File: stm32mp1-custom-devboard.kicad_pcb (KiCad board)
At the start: 4 copper layers, 120 x 72 mm, 124 parts, among them Con1 52746-0671, Con2 505110-2491, Con3 2041119-1, Con4 USB_C_Wurth_632723130112, Con5 USB_C_Wurth_632723130112, P1 Main Power Supply, Q1 BC847B, T2 WE-RJ45_74990101210, U1 TPS61169DCKR, U2 MCP1703T-3302E, U3 ST1S10PHR, U4 ST1S09IPUR, U5 STM32F103C(8-B)Tx, U6 MCP1700T-3302E_MB, U7 KSZ8041NL_RNL, X1 8.000MHZ, X2 ECS-2016MV-250-CN-TR

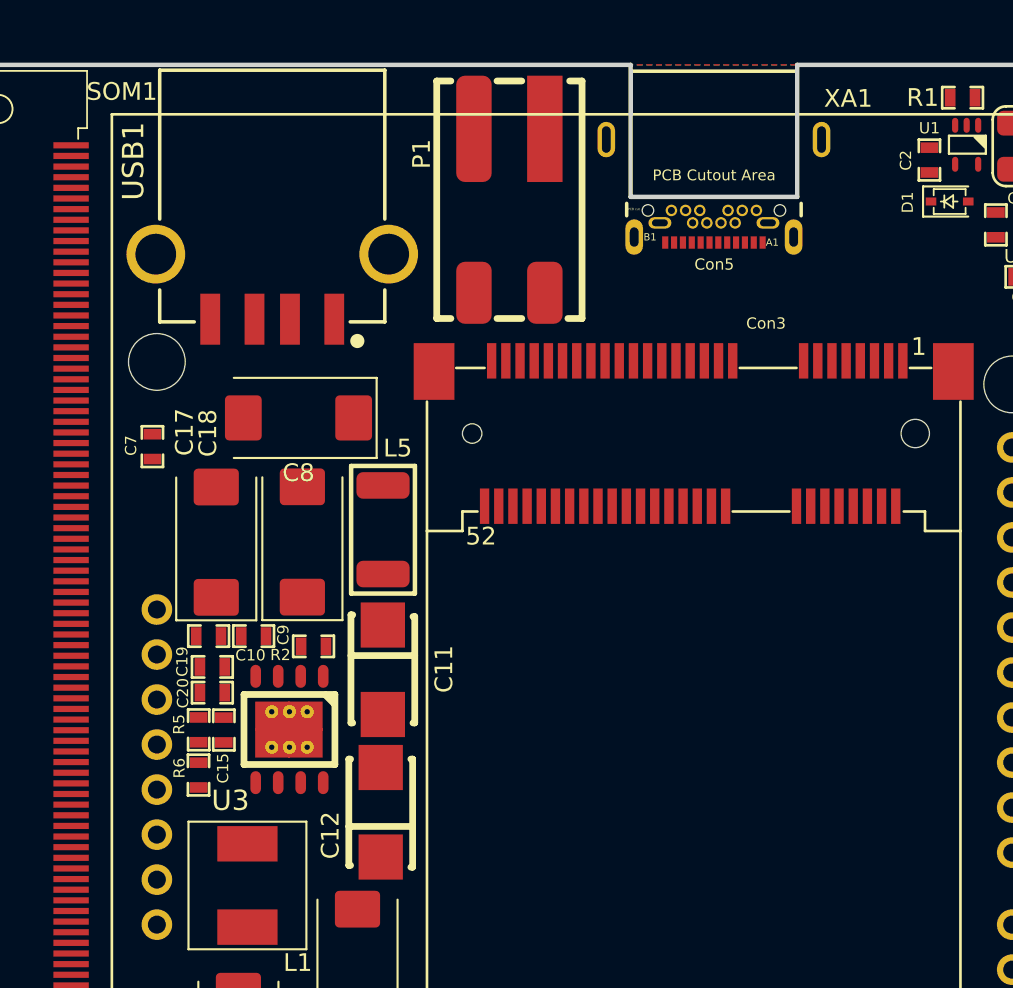
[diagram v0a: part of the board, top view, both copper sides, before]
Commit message: Updated schematic, added some components, figurated components on pcb
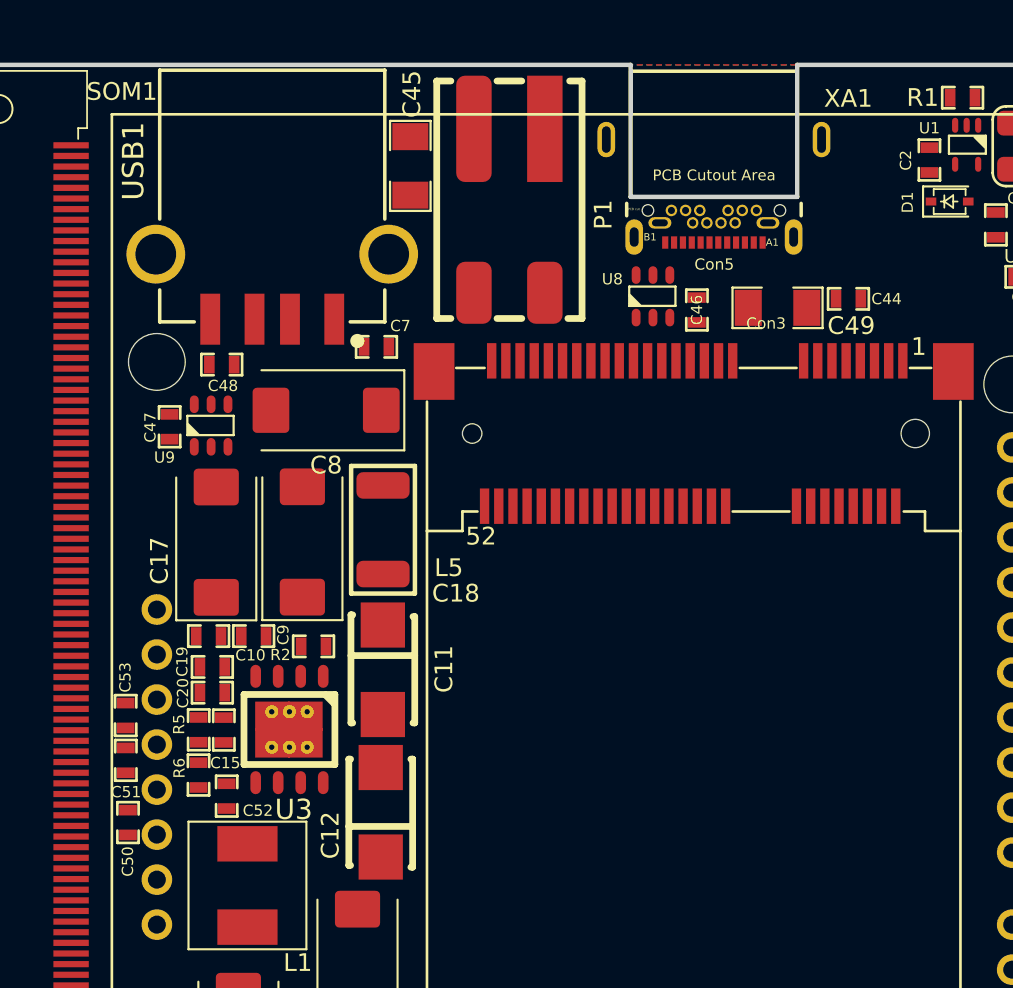
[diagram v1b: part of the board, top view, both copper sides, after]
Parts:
- added C44: 10uF, Capacitors_Smd_0603:10uF_10V_0603, F.Cu at (172.8, 79.6)
- added C45: 1nF/2kV, Capacitors_Smd_1206:1nF_2kV_1206, F.Cu at (148.0, 72.1)
- added C46: 100n, Capacitors_Smd_0603:100nF_0603, F.Cu at (164.2, 80.2)
- added C47: 10uF, Capacitors_Smd_0603:10uF_10V_0603, F.Cu at (134.5, 86.8)
- added C48: 100n, Capacitors_Smd_0603:100nF_0603, F.Cu at (137.4, 83.3)
- added C49: 1nF/2kV, Capacitors_Smd_1206:1nF_2kV_1206, F.Cu at (168.8, 80.1)
- added C50: 10uF, Capacitors_Smd_0603:10uF_10V_0603, F.Cu at (132.1, 109.2)
- added C51: 10uF, Capacitors_Smd_0603:10uF_10V_0603, F.Cu at (132.0, 105.7)
- added C52: 100n, Capacitors_Smd_0603:100nF_0603, F.Cu at (137.7, 107.7)
- added C53: 100n, Capacitors_Smd_0603:100nF_0603, F.Cu at (132.0, 103.1)
- added U8: USBLC6-2, ESD_Protectors:USBLC6-2_SOT23-6L, F.Cu at (161.7, 79.5)
- added U9: USBLC6-2, ESD_Protectors:USBLC6-2_SOT23-6L, F.Cu at (136.8, 86.8)
- moved C7 13.8 mm to (146.1, 82.3), turned to 180 degrees
- moved C8 1.62 mm to (143.3, 85.9)
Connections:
- net SHDN renamed Net-(C26-Pad2)
- C13 pad 1: /Power Supply Module/POWER_IN_7_TO_18V -> VPP
- C14 pad 1: /Power Supply Module/POWER_IN_7_TO_18V -> VPP
- C7 pad 1: /Power Supply Module/POWER_IN_7_TO_18V -> VPP
- C8 pad 1: /Power Supply Module/POWER_IN_7_TO_18V -> VPP
- Con5 pad A1: (no net) -> GND
- Con5 pad A12: (no net) -> GND
- Con5 pad A4: (no net) -> 5V
- Con5 pad A6: (no net) -> Net-(Con5-PadA6)
- Con5 pad A7: (no net) -> Net-(Con5-PadA7)
- Con5 pad A9: (no net) -> 5V
- Con5 pad B1: (no net) -> GND
- Con5 pad B12: (no net) -> GND
- Con5 pad B4: (no net) -> 5V
- Con5 pad B6: (no net) -> Net-(Con5-PadA6)
- Con5 pad B7: (no net) -> Net-(Con5-PadA7)
- Con5 pad B9: (no net) -> 5V
- Con5 pad S1: (no net) -> Net-(C49-Pad2)
- Con5 pad S2: (no net) -> Net-(C49-Pad2)
- Con5 pad S3: (no net) -> Net-(C49-Pad2)
- Con5 pad S4: (no net) -> Net-(C49-Pad2)
- L5 pad 1: /Power Supply Module/POWER_IN_7_TO_18V -> VPP
- P1 pad 2: /Power Supply Module/POWER_IN_7_TO_18V -> VPP
- U4 pad 4: /Power Supply Module/POWER_IN_7_TO_18V -> VPP
- U4 pad 5: /Power Supply Module/POWER_IN_7_TO_18V -> VPP
- U4 pad 6: /Power Supply Module/POWER_IN_7_TO_18V -> VPP
- USB1 pad 1: (no net) -> 5V
- USB1 pad 2: (no net) -> Net-(U9-Pad6)
- USB1 pad 3: (no net) -> Net-(U9-Pad4)
- USB1 pad 4: (no net) -> GND
- XA1 pad 3V3: (no net) -> 3V3
- XA1 pad 5V1: (no net) -> 5V
- XA1 pad 5V2: (no net) -> 5V
- XA1 pad GND1: (no net) -> GND
- XA1 pad GND2: (no net) -> GND
- XA1 pad GND3: (no net) -> GND
- XA1 pad GND4: (no net) -> GND
- XA1 pad VIN: (no net) -> VPP

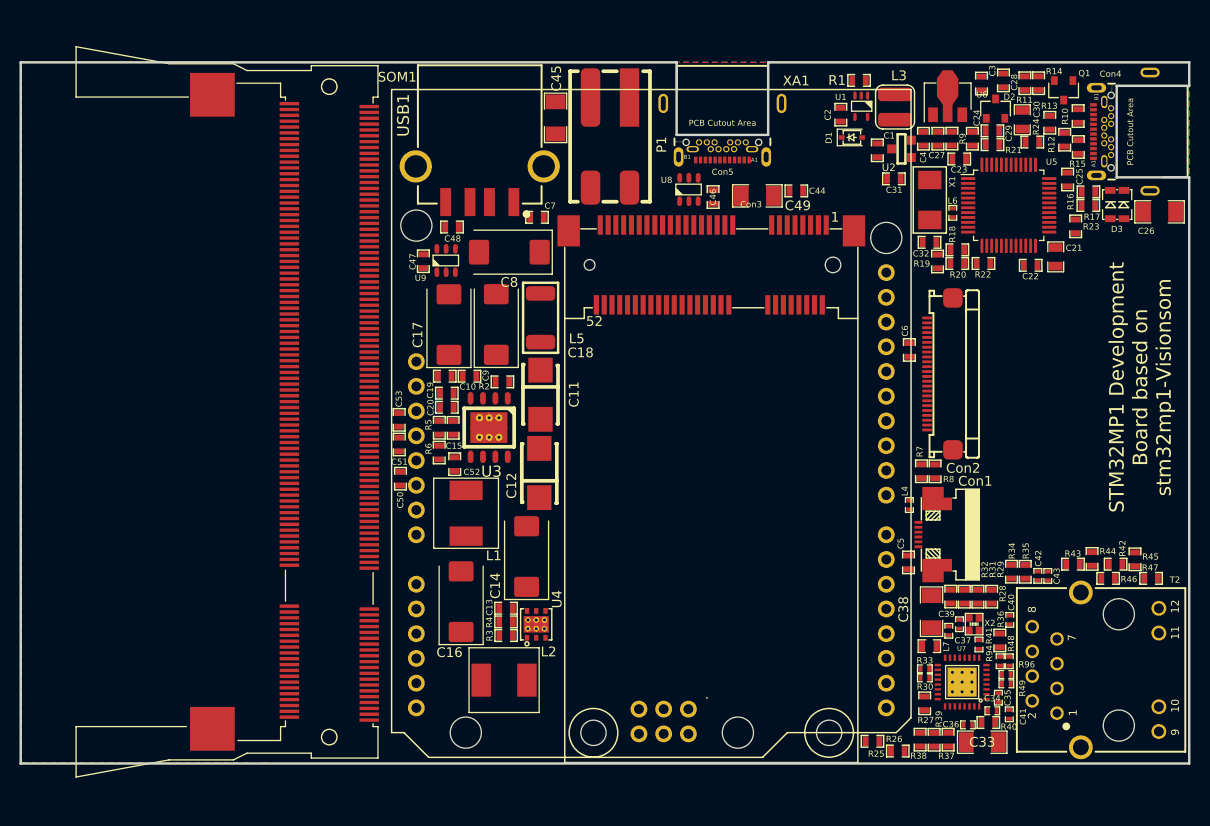
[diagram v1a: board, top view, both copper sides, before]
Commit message: Schematic work contiune, added pinout spreadsheet
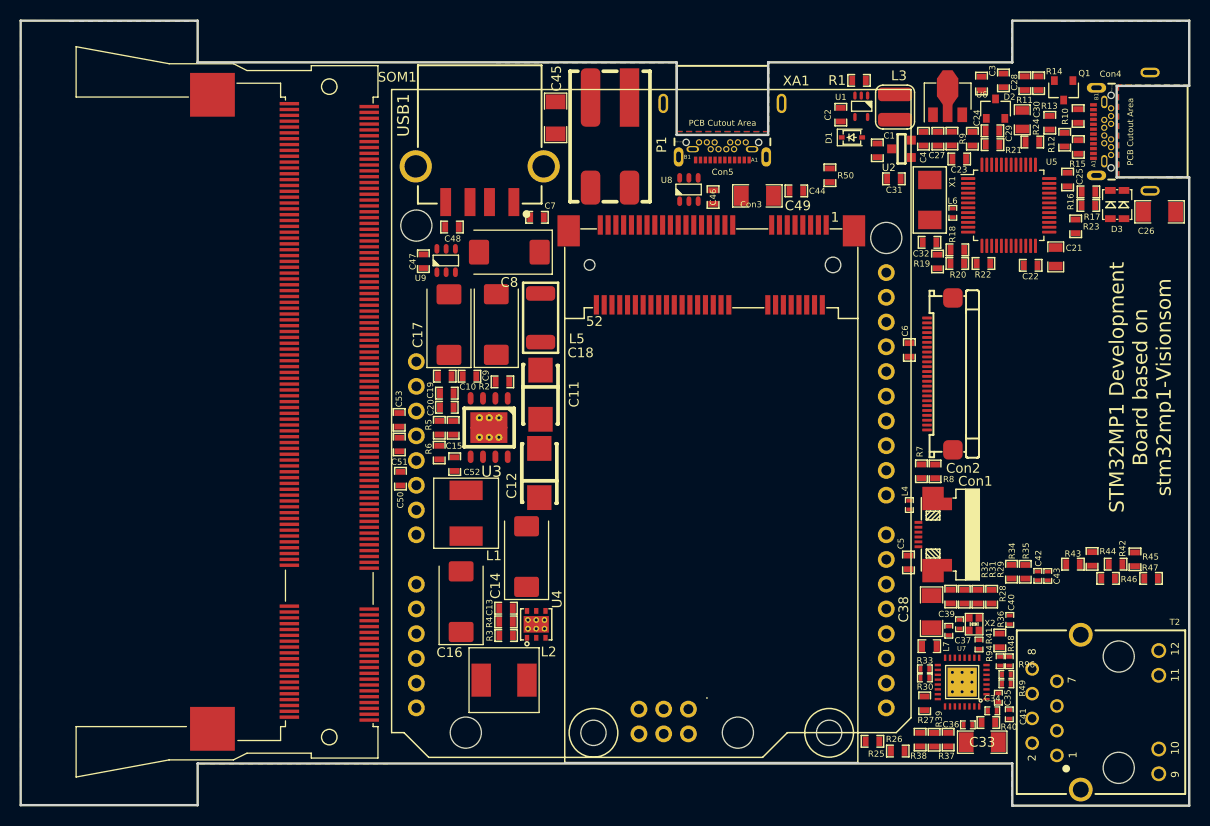
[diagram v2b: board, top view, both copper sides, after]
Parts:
- added R50: 47k, Resistor_Smd_0603:47k_0603, F.Cu at (176.2, 78.0)
- moved T2 4.34 mm to (205.9, 133.1)
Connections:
- Con5 pad A5: (no net) -> /USB Module/USB-C-ID
- Con5 pad B5: (no net) -> /USB Module/USB-C-ID
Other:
- board size 120 x 72 mm -> 120 x 80.6 mm
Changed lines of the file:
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@@
   (general
     (thickness 1.6)
-    (drawings 13)
+    (drawings 21)
     (tracks 0)
     (zones 0)
-    (modules 136)
-    (nets 91)
+    (modules 137)
+    (nets 92)
   )
   (page A4)
@@
     (38 B.Mask user)
     (39 F.Mask user)
-    (40 Dwgs.User user hide)
+    (40 Dwgs.User user)
     (41 Cmts.User user)
     (42 Eco1.User user)
@@
   (net 89 "Net-(U9-Pad6)")
   (net 90 "Net-(C45-Pad2)")
+  (net 91 "/USB Module/USB-C-ID")
   (net_class Default "This is the default net class."
     (clearance 0.2)
@@
     (add_net "/STM32MP1 module/PE2_I2C4_SDA")
     (add_net "/STM32MP1 module/PF10_GPIO")
+    (add_net "/USB Module/USB-C-ID")
     (add_net 3V3)
     (add_net 5V)
@@
   )
   (module RJ45_Ethernet_Transformer:WE-RJ45_74990101210 (layer F.Cu)
-    (at 205.88 128.8 90)
+    (at 205.87 133.14 90)
     (descr "WE-RJ45 LAN TRANSFORMER")
     (tags "WE-RJ45 LAN TRANSFORMER")
@@
       (net 13 5V) (solder_mask_margin 0.05) (solder_paste_margin_ratio -0.09) (clearance 0.03))
     (pad A5 smd rect (at -0.7493 -4.57454 180) (size 0.35 0.7) (layers F.Cu F.Paste F.Mask)
-      (solder_mask_margin 0.05) (solder_paste_margin_ratio -0.09) (clearance 0.03))
+      (net 91 "/USB Module/USB-C-ID") (solder_mask_margin 0.05) (solder_paste_margin_ratio -0.09) (clearance 0.03))
     (pad A6 smd rect (at -0.24892 -4.57454 180) (size 0.35 0.7) (layers F.Cu F.Paste F.Mask)
       (net 86 "Net-(Con5-PadA6)") (solder_mask_margin 0.05) (solder_paste_margin_ratio -0.09) (clearance 0.03))
@@
       (net 13 5V) (solder_mask_margin 0.05) (clearance 0.03))
     (pad B5 thru_hole circle (at 0.79756 -2.76352 180) (size 0.65 0.65) (drill 0.4) (layers *.Cu *.Paste *.Mask)
-      (solder_mask_margin 0.05) (clearance 0.03))
+      (net 91 "/USB Module/USB-C-ID") (solder_mask_margin 0.05) (clearance 0.03))
     (pad B6 thru_hole circle (at 0.39878 -3.46456 180) (size 0.65 0.65) (drill 0.4) (layers *.Cu *.Paste *.Mask)
       (net 86 "Net-(Con5-PadA6)") (solder_mask_margin 0.05) (clearance 0.03))
@@
     )
   )
-  (gr_line (start 169.87 66.41) (end 213.11 66.41) (layer Edge.Cuts) (width 0.25))
+  (module Resistor_Smd_0603:47k_0603 (layer F.Cu)
+    (at 176.21 78 90)
+    (descr "Vishay SMD SM0603")
+    (tags Resistor)
+    (solder_paste_margin -0.06)
+    (attr smd)
+    (fp_text reference R50 (at -0.03 1.62 180) (layer F.SilkS)
+      (effects (font (size 0.635 0.635) (thickness 0.127)))
+    )
+    (fp_text value 47k (at 0 0 90) (layer F.SilkS) hide
+      (effects (font (size 0.635 0.635) (thickness 0.127)))
+    )
+    (fp_line (start -0.45 -0.6) (end -1.15 -0.6) (layer F.SilkS) (width 0.15))
+    (fp_line (start -1.15 -0.6) (end -1.15 0.6) (layer F.SilkS) (width 0.15))
+    (fp_line (start -1.15 0.6) (end -0.45 0.6) (layer F.SilkS) (width 0.15))
+    (fp_line (start 0.45 -0.6) (end 1.15 -0.6) (layer F.SilkS) (width 0.15))
+    (fp_line (start 1.15 -0.6) (end 1.15 0.6) (layer F.SilkS) (width 0.15))
+    (fp_line (start 1.15 0.6) (end 0.45 0.6) (layer F.SilkS) (width 0.15))
+    (pad 1 smd rect (at -0.7 0 90) (size 0.6 1) (layers F.Cu F.Paste F.Mask)
+      (net 13 5V) (solder_mask_margin 0.01) (clearance 0.03))
+    (pad 2 smd rect (at 0.7 0 90) (size 0.6 1) (layers F.Cu F.Paste F.Mask)
+      (net 91 "/USB Module/USB-C-ID") (solder_mask_margin 0.01) (clearance 0.03))
+    (model Resistors/Smd_0603/3D_View/47k_0603.x3d
+      (at (xyz 0 0 0))
+      (scale (xyz 1 1 1))
+      (rotate (xyz 0 0 0))
+    )
+  )
+  (gr_line (start 194.94 66.41) (end 194.94 62.13) (layer Edge.Cuts) (width 0.25))
+  (gr_line (start 213.11 62.13) (end 194.94 62.13) (layer Edge.Cuts) (width 0.25))
+  (gr_line (start 111.28 66.41) (end 111.28 62.13) (layer Edge.Cuts) (width 0.25))
+  (gr_line (start 111.28 62.13) (end 93.11 62.13) (layer Edge.Cuts) (width 0.25))
+  (gr_line (start 93.11 142.69) (end 111.28 142.69) (layer Edge.Cuts) (width 0.25))
+  (gr_line (start 111.28 138.41) (end 111.28 142.69) (layer Edge.Cuts) (width 0.25))
+  (gr_line (start 194.94 142.74) (end 213.11 142.74) (layer Edge.Cuts) (width 0.25))
+  (gr_line (start 194.94 138.41) (end 194.94 142.74) (layer Edge.Cuts) (width 0.25))
+  (gr_line (start 169.87 66.41) (end 194.94 66.41) (layer Edge.Cuts) (width 0.25))
   (gr_line (start 169.87 73.86) (end 169.87 66.41) (layer Edge.Cuts) (width 0.25))
   (gr_line (start 169.87 73.86) (end 160.47 73.86) (layer Edge.Cuts) (width 0.25))
@@
   (gr_line (start 205.66 68.82) (end 213.11 68.82) (layer Edge.Cuts) (width 0.25))
   (gr_line (start 205.66 78.22) (end 213.11 78.22) (layer Edge.Cuts) (width 0.25))
-  (gr_line (start 213.11 78.22) (end 213.11 138.41) (layer Edge.Cuts) (width 0.25))
+  (gr_line (start 213.11 78.22) (end 213.11 142.74) (layer Edge.Cuts) (width 0.25))
   (gr_text "STM32MP1 Development\nBoard based on \nstm32mp1-Visionsom" (at 208.1 99.78 90) (layer F.SilkS)
     (effects (font (size 1.5 1.5) (thickness 0.3)))
   )
-  (gr_line (start 93.11 138.41) (end 213.11 138.41) (layer Edge.Cuts) (width 0.25))
-  (gr_line (start 93.11 66.41) (end 93.11 138.41) (layer Edge.Cuts) (width 0.25))
-  (gr_line (start 213.11 66.41) (end 213.11 68.82) (layer Edge.Cuts) (width 0.25))
-  (gr_line (start 93.11 66.41) (end 160.47 66.41) (layer Edge.Cuts) (width 0.25))
+  (gr_line (start 111.28 138.41) (end 194.94 138.41) (layer Edge.Cuts) (width 0.25))
+  (gr_line (start 93.11 62.13) (end 93.11 142.69) (layer Edge.Cuts) (width 0.25))
+  (gr_line (start 213.11 62.13) (end 213.11 68.82) (layer Edge.Cuts) (width 0.25))
+  (gr_line (start 111.28 66.41) (end 160.47 66.41) (layer Edge.Cuts) (width 0.25))
   (zone (net 1) (net_name GND) (layer F.Cu) (hatch edge 0.508)
-    (connect_pads (clearance 0.254))
+    (connect_pads yes (clearance 0.254))
     (min_thickness 0.254)
     (fill yes (arc_segments 32) (thermal_gap 0.508) (thermal_bridge_width 0.508))
     (polygon
       (pts
-        (xy 213.11 138.42) (xy 93.11 138.39) (xy 93.11 66.41) (xy 213.12 66.41)
+        (xy 213.11 62.13) (xy 213.11 68.72) (xy 205.84 68.7) (xy 205.88 78.25) (xy 213.12 78.23)
+        (xy 213.11 142.74) (xy 194.93 142.75) (xy 194.93 138.41) (xy 111.29 138.42) (xy 111.28 142.7)
+        (xy 93.1 142.69) (xy 93.1 62.12) (xy 111.28 62.13) (xy 111.27 66.4) (xy 160.46 66.43)
+        (xy 160.46 73.51) (xy 169.94 73.52) (xy 169.93 66.41) (xy 194.93 66.4) (xy 194.94 62.12)
       )
     )
   )
-  (zone (net 11) (net_name 3V3) (layer In1.Cu) (hatch edge 0.508)
-    (connect_pads (clearance 0.254))
+  (zone (net 1) (net_name GND) (layer B.Cu) (hatch edge 0.508)
+    (connect_pads yes (clearance 0.254))
     (min_thickness 0.254)
     (fill yes (arc_segments 32) (thermal_gap 0.508) (thermal_bridge_width 0.508))
     (polygon
       (pts
-        (xy 213.11 138.4) (xy 93.11 138.41) (xy 93.11 66.41) (xy 213.12 66.41)
+        (xy 213.11 62.13) (xy 213.11 68.72) (xy 205.84 68.7) (xy 205.88 78.25) (xy 213.12 78.23)
+        (xy 213.11 142.74) (xy 194.93 142.75) (xy 194.93 138.41) (xy 111.29 138.42) (xy 111.28 142.7)
+        (xy 93.1 142.69) (xy 93.1 62.12) (xy 111.28 62.13) (xy 111.27 66.4) (xy 160.46 66.43)
+        (xy 160.46 73.51) (xy 169.94 73.52) (xy 169.93 66.41) (xy 194.93 66.4) (xy 194.94 62.12)
       )
     )
   )
   (zone (net 1) (net_name GND) (layer In2.Cu) (hatch edge 0.508)
-    (connect_pads (clearance 0.254))
+    (connect_pads yes (clearance 0.254))
     (min_thickness 0.254)
     (fill yes (arc_segments 32) (thermal_gap 0.508) (thermal_bridge_width 0.508))
     (polygon
       (pts
-        (xy 213.11 138.4) (xy 93.11 138.41) (xy 93.11 66.41) (xy 213.12 66.41)
+        (xy 213.11 62.13) (xy 213.11 68.72) (xy 205.84 68.7) (xy 205.88 78.25) (xy 213.12 78.23)
+        (xy 213.11 142.74) (xy 194.93 142.75) (xy 194.93 138.41) (xy 111.29 138.42) (xy 111.28 142.7)
+        (xy 93.1 142.69) (xy 93.1 62.12) (xy 111.28 62.13) (xy 111.27 66.4) (xy 160.46 66.43)
+        (xy 160.46 73.51) (xy 169.94 73.52) (xy 169.93 66.41) (xy 194.93 66.4) (xy 194.94 62.12)
       )
     )
   )
-  (zone (net 1) (net_name GND) (layer B.Cu) (hatch edge 0.508)
-    (connect_pads (clearance 0.254))
+  (zone (net 11) (net_name 3V3) (layer In1.Cu) (hatch edge 0.508)
+    (connect_pads yes (clearance 0.254))
     (min_thickness 0.254)
     (fill yes (arc_segments 32) (thermal_gap 0.508) (thermal_bridge_width 0.508))
     (polygon
       (pts
-        (xy 213.11 138.4) (xy 93.11 138.41) (xy 93.11 66.41) (xy 213.12 66.41)
+        (xy 213.11 62.13) (xy 213.11 68.72) (xy 205.84 68.7) (xy 205.88 78.25) (xy 213.12 78.23)
+        (xy 213.11 142.74) (xy 194.93 142.75) (xy 194.93 138.41) (xy 111.29 138.42) (xy 111.28 142.7)
+        (xy 93.1 142.69) (xy 93.1 62.12) (xy 111.28 62.13) (xy 111.27 66.4) (xy 160.46 66.43)
+        (xy 160.46 73.51) (xy 169.94 73.52) (xy 169.93 66.41) (xy 194.93 66.4) (xy 194.94 62.12)
       )
     )
